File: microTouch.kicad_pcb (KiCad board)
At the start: 2 copper layers, 26.7 x 41.9 mm, 9 parts, among them J1 SERVO, J2 PRINTER, U1 T1302

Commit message: smaller
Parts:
- moved H1 28.6 mm to (102.2, 90.2), turned to 0 degrees
- moved J2 27.4 mm to (114.3, 90.1), turned to 180 degrees
- moved H2 25.8 mm to (102.9, 112.5), turned to 0 degrees
- moved D1 21.6 mm to (106.6, 95.0), turned to 90 degrees
- moved U1 20.6 mm to (103.6, 106.4), turned to 90 degrees
- moved R1 18.6 mm to (106.6, 107.8), turned to -90 degrees
- moved R2 17.4 mm to (106.6, 103.5), turned to -90 degrees
- moved R3 16.3 mm to (106.6, 99.2), turned to -90 degrees
- moved J1 6.50 mm to (109.7, 95.2), turned to 0 degrees
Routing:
- net /SIG: track 12.3 -> 26.5 mm, vias 1 -> 2
- net /VCC: track 19.8 -> 27.1 mm
- net /SERVO: track 13.8 -> 21.0 mm
- net Net-(R1-Pad2): track 3.50 -> 7.53 mm
- net Net-(D1-Pad1): track 1.77 -> 2.38 mm
- net GND: vias 2 -> 4
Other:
- board size 26.7 x 41.9 mm -> 31.1 x 30.5 mm
- board text added: "cperiod 2021"
- board text added: "microTouch v1.0"
- board text removed: "microTouch cperiod 2021"

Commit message: assorted tweaks
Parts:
- D1: footprint LED_SMD:LED_0603_1608Metric_Pad1.05x0.95mm_HandSolder -> LED_SMD:LED_0805_2012Metric_Pad1.15x1.40mm_HandSolder
- R1, R2, R3: footprint Resistor_SMD:R_0603_1608Metric_Pad0.98x0.95mm_HandSolder -> Resistor_SMD:R_0805_2012Metric_Pad1.20x1.40mm_HandSolder
- moved U1 0.25 mm to (103.4, 106.4)
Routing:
- net Net-(R1-Pad2): track 7.53 -> 8.04 mm

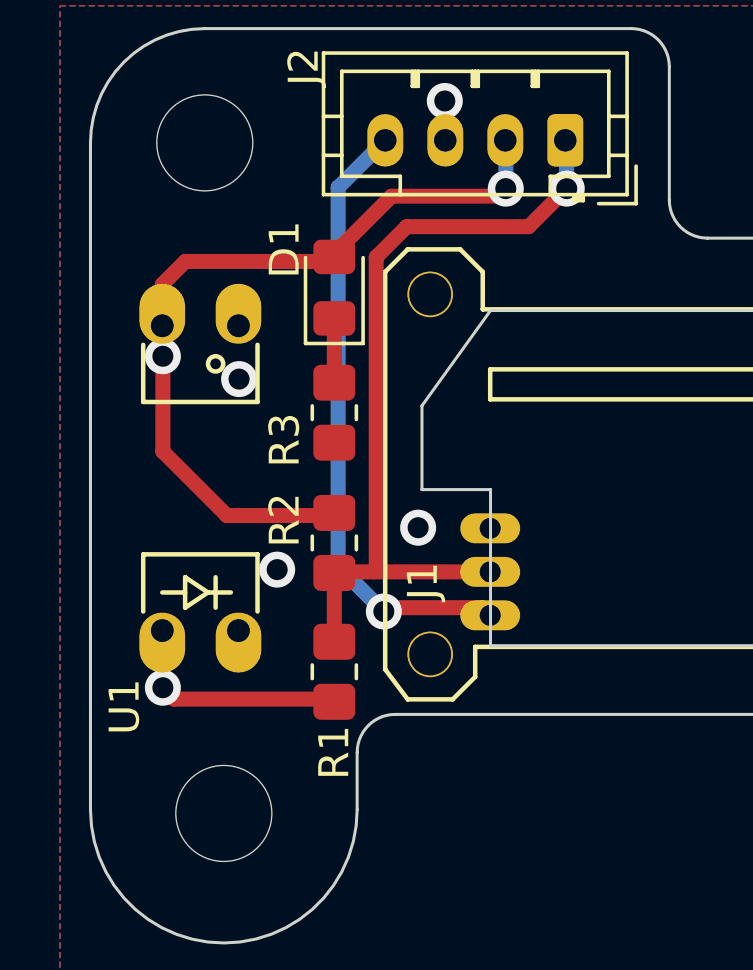
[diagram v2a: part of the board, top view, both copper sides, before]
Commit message: fix photint pinout, adjust pullup, move LED out further
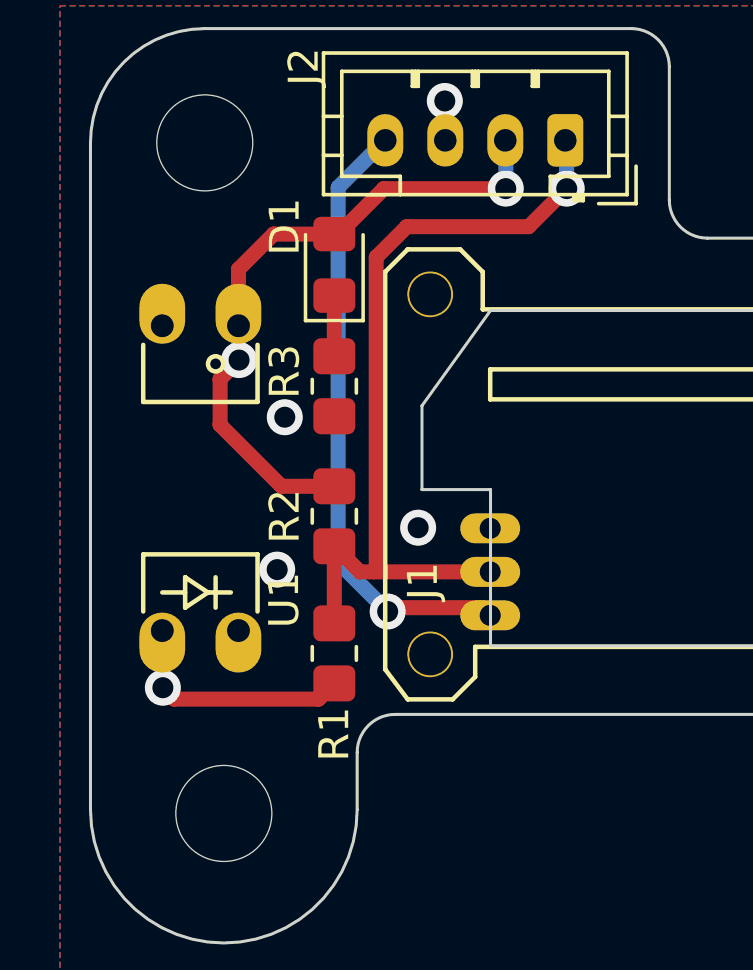
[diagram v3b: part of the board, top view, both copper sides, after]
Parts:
- U1: value T1302 -> ZOS-T1302
- moved R2 0.89 mm to (106.6, 102.6)
- moved R3 0.88 mm to (106.6, 98.3)
- moved D1 0.76 mm to (106.6, 94.2)
- moved R1 0.61 mm to (106.6, 107.2)
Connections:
- U1 pad 1: GND -> Net-(R1-Pad2)
- U1 pad 2: Net-(R1-Pad2) -> GND
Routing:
- net /SIG: track 26.7 -> 21.8 mm

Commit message: more minor tweaks
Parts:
- R2: value 1K -> 2K2
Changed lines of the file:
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@@
       (effects (font (size 1 1) (thickness 0.15)))
     )
-    (fp_text value "1K" (at 0 1.65 -90) (layer "F.Fab")
+    (fp_text value "2K2" (at 0 1.65 -90) (layer "F.Fab")
       (effects (font (size 1 1) (thickness 0.15)))
     )
@@
     (fp_line (start -1 0.625) (end -1 -0.625) (layer "F.Fab") (width 0.1))
     (pad "1" smd roundrect locked (at -1 0 270) (size 1.2 1.4) (layers "F.Cu" "F.Paste" "F.Mask") (roundrect_rratio 0.2083333333)
-      (net 2 "/SIG"))
+      (net 2 "/SIG") (pintype "passive"))
     (pad "2" smd roundrect locked (at 1 0 270) (size 1.2 1.4) (layers "F.Cu" "F.Paste" "F.Mask") (roundrect_rratio 0.2083333333)
-      (net 4 "/VCC"))
+      (net 4 "/VCC") (pintype "passive"))
     (model "${KICAD6_3DMODEL_DIR}/Resistor_SMD.3dshapes/R_0805_2012Metric.wrl"
       (offset (xyz 0 0 0))
@@
     (fp_line (start -1 0.625) (end -1 -0.625) (layer "F.Fab") (width 0.1))
     (pad "1" smd roundrect locked (at -1 0 270) (size 1.2 1.4) (layers "F.Cu" "F.Paste" "F.Mask") (roundrect_rratio 0.2083333333)
-      (net 1 "Net-(D1-Pad1)"))
+      (net 1 "Net-(D1-Pad1)") (pintype "passive"))
     (pad "2" smd roundrect locked (at 1 0 270) (size 1.2 1.4) (layers "F.Cu" "F.Paste" "F.Mask") (roundrect_rratio 0.2083333333)
-      (net 5 "GND"))
+      (net 5 "GND") (pintype "passive"))
     (model "${KICAD6_3DMODEL_DIR}/Resistor_SMD.3dshapes/R_0805_2012Metric.wrl"
       (offset (xyz 0 0 0))

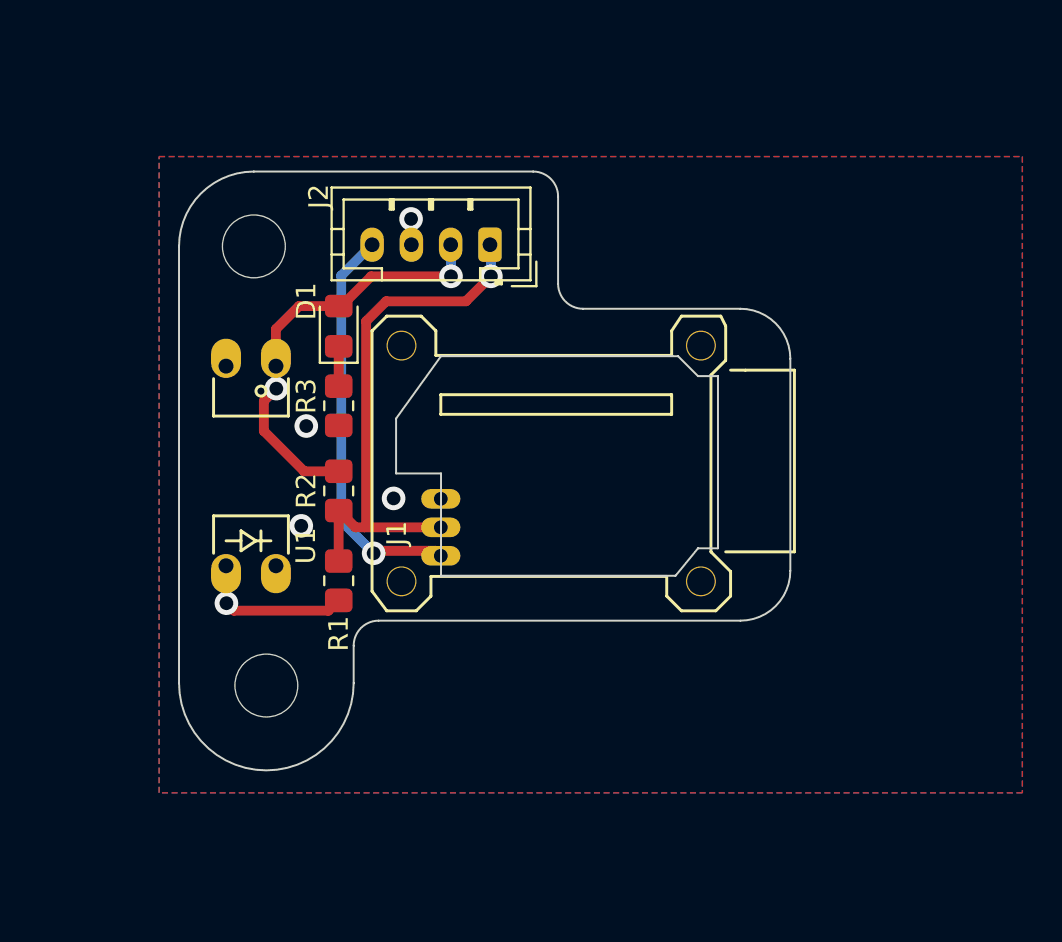
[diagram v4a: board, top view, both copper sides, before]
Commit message: redesign with a A3144 hall effect sensor
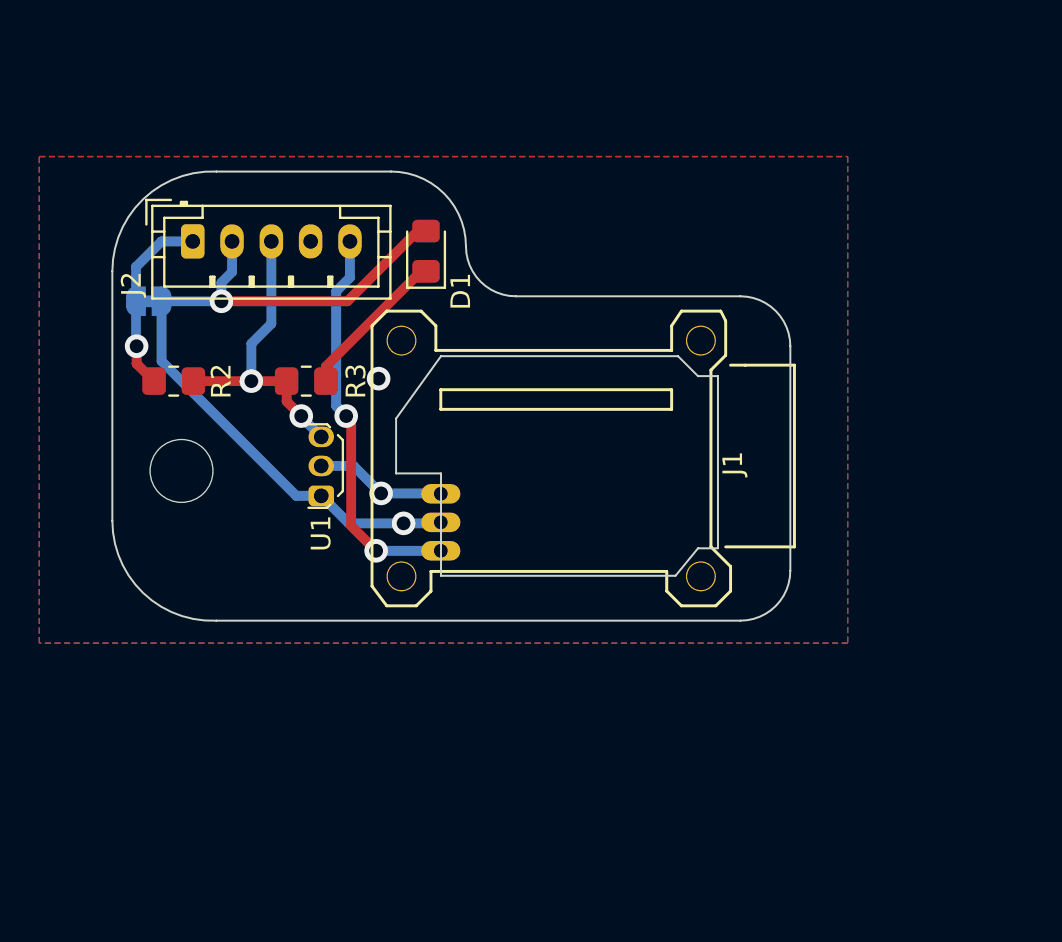
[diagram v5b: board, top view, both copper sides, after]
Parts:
- removed H2: MountingHole, MountingHole:MountingHole_3.2mm_M3
- removed R1: 220, Resistor_SMD:R_0805_2012Metric_Pad1.20x1.40mm_HandSolder
- added JP1: LOGICV, Jumper:SolderJumper-2_P1.3mm_Bridged_RoundedPad1.0x1.5mm, B.Cu at (96.9, 93.0)
- J2: footprint Connector_JST:JST_PH_B4B-PH-K_1x04_P2.00mm_Vertical -> Connector_JST:JST_PH_B5B-PH-K_1x05_P2.00mm_Vertical
- R2, R3: value 2K2 -> 4K7
- U1: value ZOS-T1302 -> A3144; footprint microTouch:T1302 -> Package_TO_SOT_THT:TO-92Flat
- moved J2 15.1 mm to (99.1, 89.9), turned to 0 degrees
- moved H1 12.0 mm to (98.6, 101.6)
- moved R2 10.1 mm to (98.2, 97.0), turned to 180 degrees
- moved D1 5.86 mm to (111.0, 90.4)
- moved U1 4.45 mm to (105.7, 102.6)
- moved R3 2.07 mm to (104.9, 97.0), turned to 0 degrees
- moved J1 0.25 mm to (109.7, 95.0)
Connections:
- D1 pad 2: /SIG -> /5V
- J1 pad 2: /VCC -> /5V
- J2 pad 1: /VCC -> /VSIG
- J2 pad 2: /SIG -> /5V
- J2 pad 3: GND -> /SIG
- J2 pad 4: /SERVO -> GND
- R2 pad 2: /VCC -> /VSIG
- R3 pad 1: Net-(D1-Pad1) -> /SIG
- R3 pad 2: GND -> Net-(D1-Pad1)
- U1 pad 1: Net-(R1-Pad2) -> /5V
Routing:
- net /5V: track 0.00 -> 38.9 mm, vias 0 -> 2
- net /VCC: track 27.6 -> 0.00 mm, vias 1 -> 0
- net /VSIG: track 0.00 -> 9.62 mm, vias 0 -> 1
- net Net-(R1-Pad2): track 8.00 -> 0.00 mm, vias 1 -> 0
- net GND: track 0.00 -> 6.67 mm, vias 4 -> 2
- net /SIG: track 21.8 -> 15.8 mm
- net Net-(D1-Pad1): track 2.15 -> 7.85 mm
- net /SERVO: track 20.6 -> 20.2 mm, vias 1 -> 2
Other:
- board size 31.1 x 30.5 mm -> 34.5 x 22.9 mm
- board text added: "microTouch v1.1"
- board text removed: "GND"
- board text removed: "SIG"
- board text removed: "SRV"
- board text removed: "VCC"
- board text removed: "microTouch v1.0"

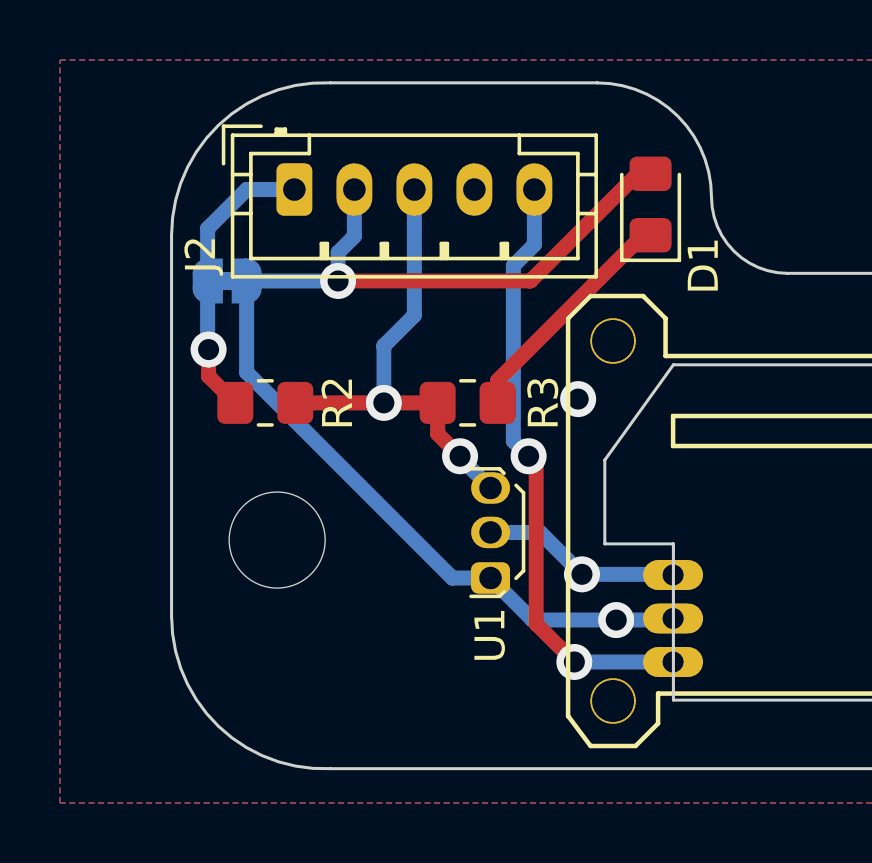
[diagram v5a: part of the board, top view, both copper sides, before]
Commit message: move some stuff around, add some filter caps for noise
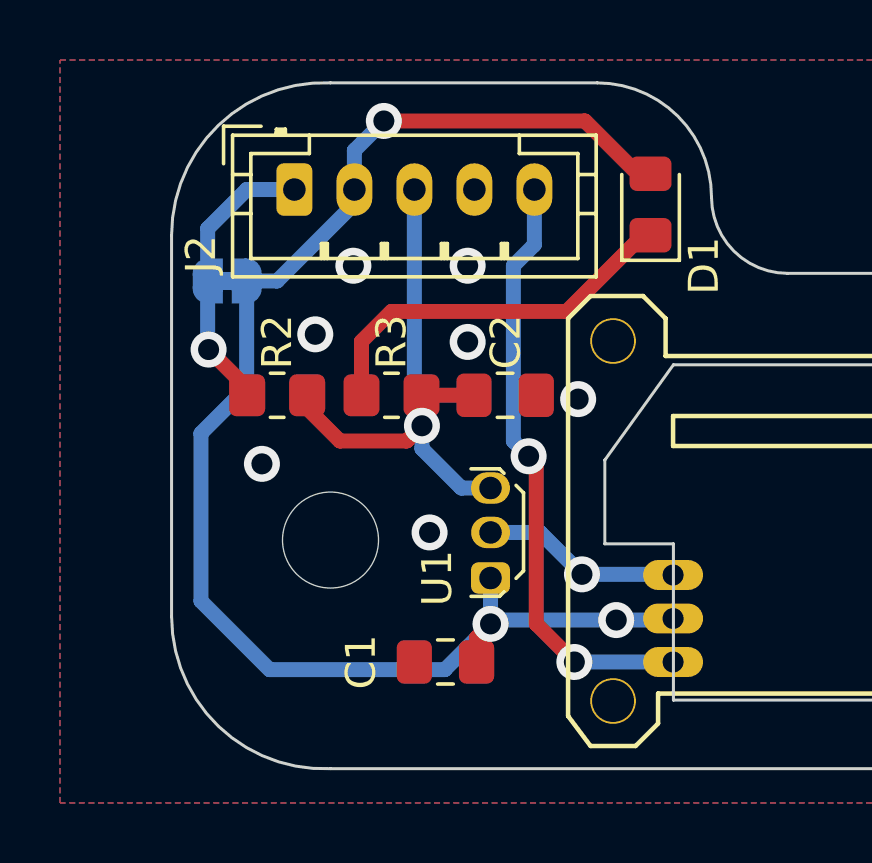
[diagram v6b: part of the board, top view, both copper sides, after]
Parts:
- added C1: 10uF, Capacitor_SMD:C_0805_2012Metric_Pad1.18x1.45mm_HandSolder, F.Cu at (104.2, 105.7)
- added C2: 100nF, Capacitor_SMD:C_0805_2012Metric_Pad1.18x1.45mm_HandSolder, F.Cu at (106.2, 96.8)
- moved R3 2.55 mm to (102.4, 96.8), turned to 180 degrees
- moved H1 1.78 mm to (100.3, 101.6)
- moved R2 0.47 mm to (98.6, 96.8)
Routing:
- net /5V: track 38.9 -> 50.5 mm, vias 2 -> 3
- net Net-(D1-Pad1): track 7.85 -> 12.9 mm
- net /SIG: track 15.8 -> 18.2 mm, vias 2 -> 1
- net GND: vias 2 -> 8
